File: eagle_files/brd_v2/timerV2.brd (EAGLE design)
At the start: 99.4 x 44.6 mm, 46 parts, among them IC1 7805T, IC6 DS1307, U1 ATMEGA328P

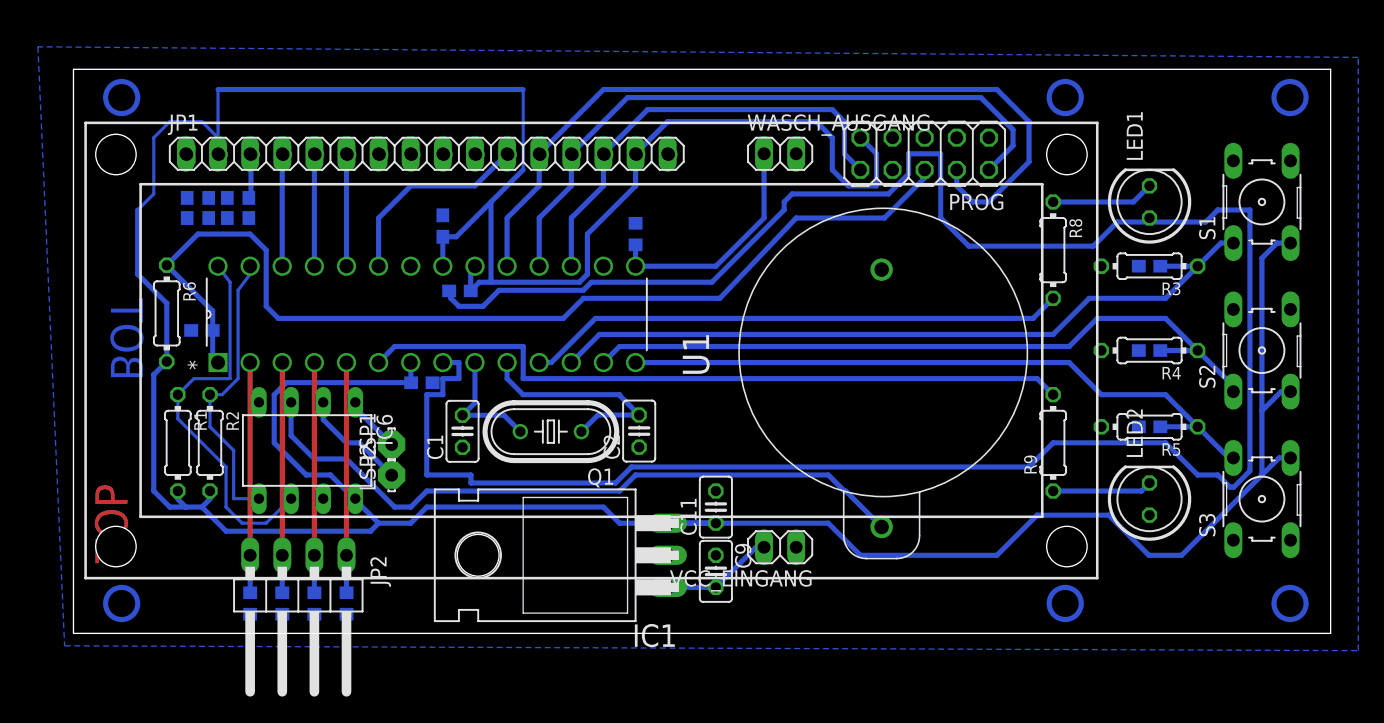
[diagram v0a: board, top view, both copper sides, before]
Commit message: added more input pins removed voltage regulator added pinheader
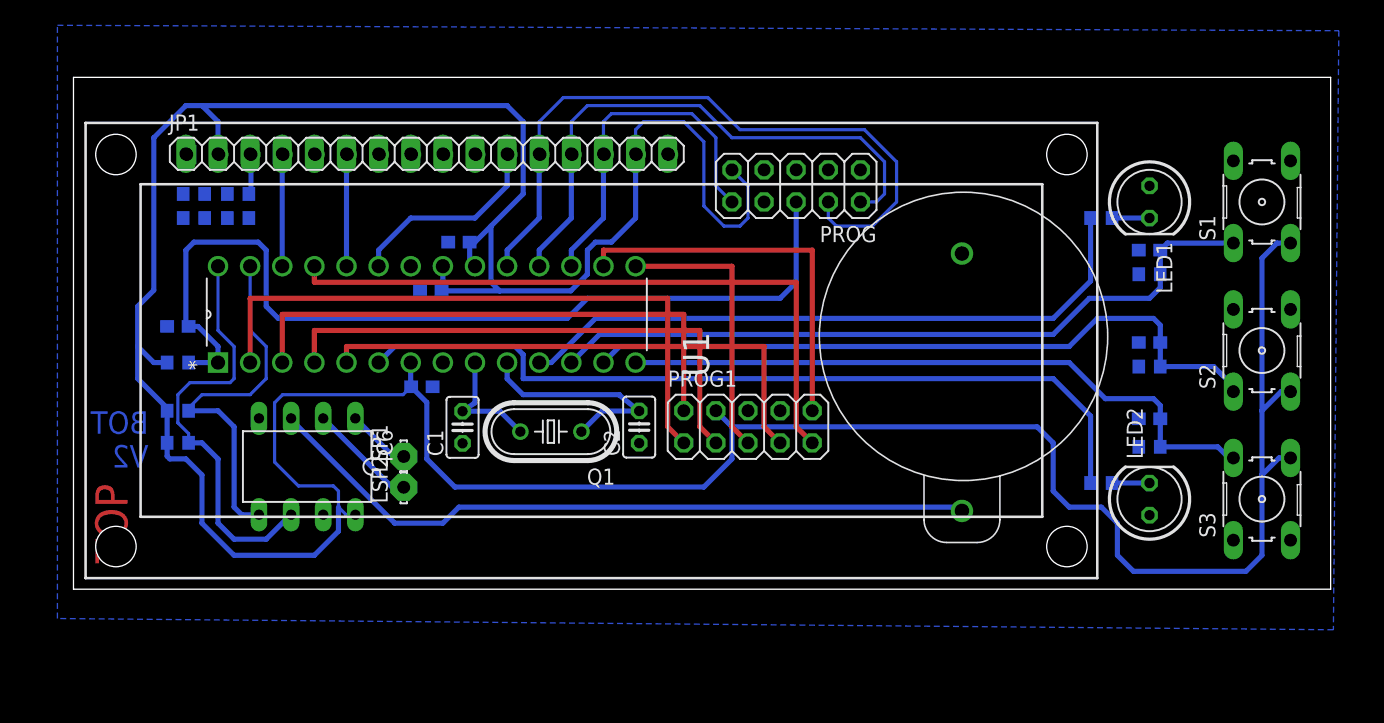
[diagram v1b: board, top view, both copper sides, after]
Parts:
- removed C11: 22 uF, resistor:C025-025X050
- removed C9: 22uF, resistor:C025-025X050
- removed IC1: 7805T, linear:TO220H
- removed JP2: (no value), pinhead:1X04/90
- removed R14, R15, R16, R17, R7: (no value), eagle-ltspice:R0603
- removed R9: 10k, resistor:0204/7
- removed VCC_EINGANG, WASCH_AUSGANG: (no value), pinhead:1X02
- added PROG1: (no value), pinhead:2X05
- added R20: (no value), eagle-ltspice:R0603
- R1, R2, R3, R4, R6: value 10k -> (none); device resistor:0204/7 -> eagle-ltspice:R0603
- R5, R8: value 10k -> 105; device resistor:0204/7 -> eagle-ltspice:R0603
- moved R6 77.8 mm to (86.4, 28.6), flipped to the bottom, turned to 0 degrees
- moved PROG 10.5 mm to (58.4, 35.6)
- moved R3 7.94 mm to (86.4, 21.3), flipped to the bottom, turned to 0 degrees
- moved R4 7.62 mm to (86.4, 14.9), flipped to the bottom, turned to 0 degrees
- moved U$1 6.48 mm to (71.5, 24.9)
- moved R1 6.35 mm to (9.53, 21.6), flipped to the bottom, turned to 180 degrees
- moved R5 5.85 mm to (82.5, 12.1), flipped to the bottom
- moved C10 5.17 mm to (29.5, 27.3), turned to 0 degrees
- moved R8 4.58 mm to (82.5, 33.0), flipped to the bottom, turned to 180 degrees
- moved C4 3.86 mm to (31.8, 31.1)
- moved R2 3.59 mm to (9.53, 17.8), flipped to the bottom, turned to 180 degrees
- moved C3 1.93 mm to (9.53, 24.4)
- moved LSP1 1.35 mm to (27.4, 14.2)
- moved LSP2 1.35 mm to (27.4, 11.7)
- moved C6 1.27 mm to (86.4, 30.5)
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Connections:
- removed net N$7: C9.2, IC1.1, VCC_EINGANG.2
- new net N$6: PROG1.10, U1.16
- net GND: now also JP1.5, PROG1.6, R6.2, U$2.5; no longer C11.2, C9.1, IC1.2, R14.1, R15.1, R16.1, R17.1, R5.2, R7.2, VCC_EINGANG.1, WASCH_AUSGANG.2
- net N$1: now also LED2.K, R5.2; no longer LED1.K, R8.1
- net N$11: now also R4.1; no longer R5.1
- net N$12: now also PROG1.7; no longer JP2.1, R17.2
- net N$13: now also R8.1; no longer R8.2
- net N$14: now also R5.1; no longer R9.2
- net N$15: now also PROG1.1; no longer JP2.4, R14.2
- net N$17: now also PROG1.3; no longer JP2.2, R16.2
- net N$20: now also R6.1; no longer R3.1
- net N$3: now also PROG1.5; no longer R7.1, WASCH_AUSGANG.1
- net N$39: now also R20.2; no longer R1.1
- net N$4: now also LED1.K, R8.2; no longer LED2.K, R9.1
- net N$40: now also R2.2; no longer R2.1
- net N$5: now also R1.2; no longer R6.1
- net N$8: now also R3.1; no longer R4.1
- net N$9: now also PROG1.2; no longer JP2.3, R15.2
- net RW: now also PROG1.9; no longer JP1.5, U$2.5
- net VCC: now also PROG1.4, R1.1, R2.1, R20.1; no longer C11.1, IC1.3, R1.2, R2.2, R6.2
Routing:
- net GND: track 179.9 -> 0.00 mm
- net RW: track 8.98 -> 52.6 mm
- net N$15: track 18.2 -> 50.1 mm
- net N$6: track 0.00 -> 30.5 mm
- net N$9: track 18.2 -> 43.2 mm
- net N$17: track 18.2 -> 42.4 mm
- net N$12: track 18.2 -> 42.4 mm
- net DB5: track 63.9 -> 54.6 mm
- net N$7: track 8.94 -> 0.00 mm
- net N$14: track 56.9 -> 65.5 mm
- net N$13: track 42.7 -> 51.3 mm
- net DB6: track 51.8 -> 44.4 mm
- net N$5: track 81.0 -> 73.9 mm
- net DB7: track 35.3 -> 28.1 mm
- net N$40: track 23.0 -> 29.4 mm
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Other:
- board size 99.4 x 44.6 mm -> 99.4 x 40.5 mm
- board text added: "BOT V2"
- board text removed: "BOT"

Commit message: Added Pulldown resistors for input pins
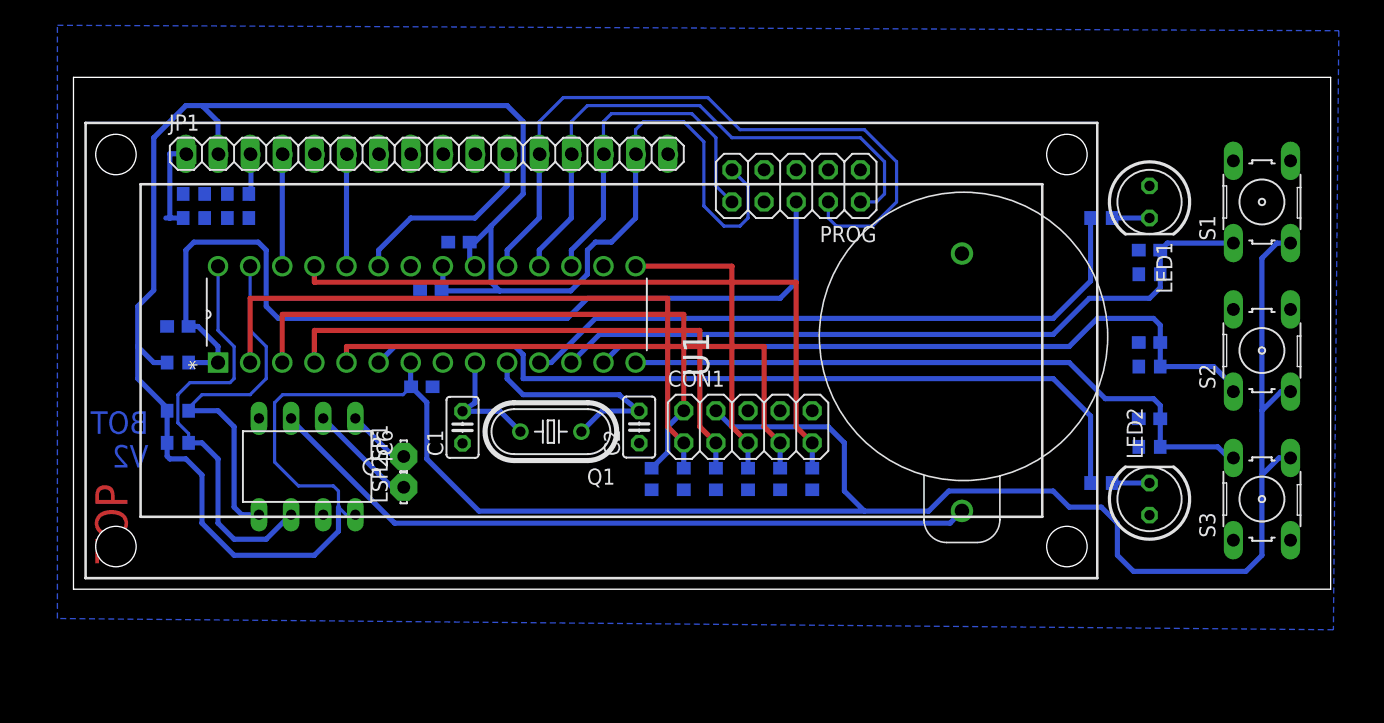
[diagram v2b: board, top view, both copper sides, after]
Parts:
- added R14, R15, R16, R17, R7, R9: 105, eagle-ltspice:R0603
- renumbered PROG1 to CON1
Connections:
- removed net N$6: CON1.10, U1.16
- net GND: now also R14.2, R15.2, R16.2, R17.2, R7.2, R9.2
- net N$12: now also R9.1
- net N$15: now also R16.1
- net N$17: now also R14.1
- net N$3: now also R17.1
- net N$9: now also R15.1
- net RW: now also R7.1
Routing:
- net N$6: track 30.5 -> 0.00 mm
- net VCC: track 300.2 -> 309.3 mm
- net GND: track 0.00 -> 7.72 mm
- net N$9: track 43.2 -> 48.8 mm
- net RW: track 52.6 -> 54.6 mm
- net N$3: track 22.1 -> 24.1 mm
- net N$17: track 42.4 -> 44.4 mm
- net N$15: track 50.1 -> 52.1 mm
- net N$12: track 42.4 -> 44.4 mm

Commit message: changed board layout
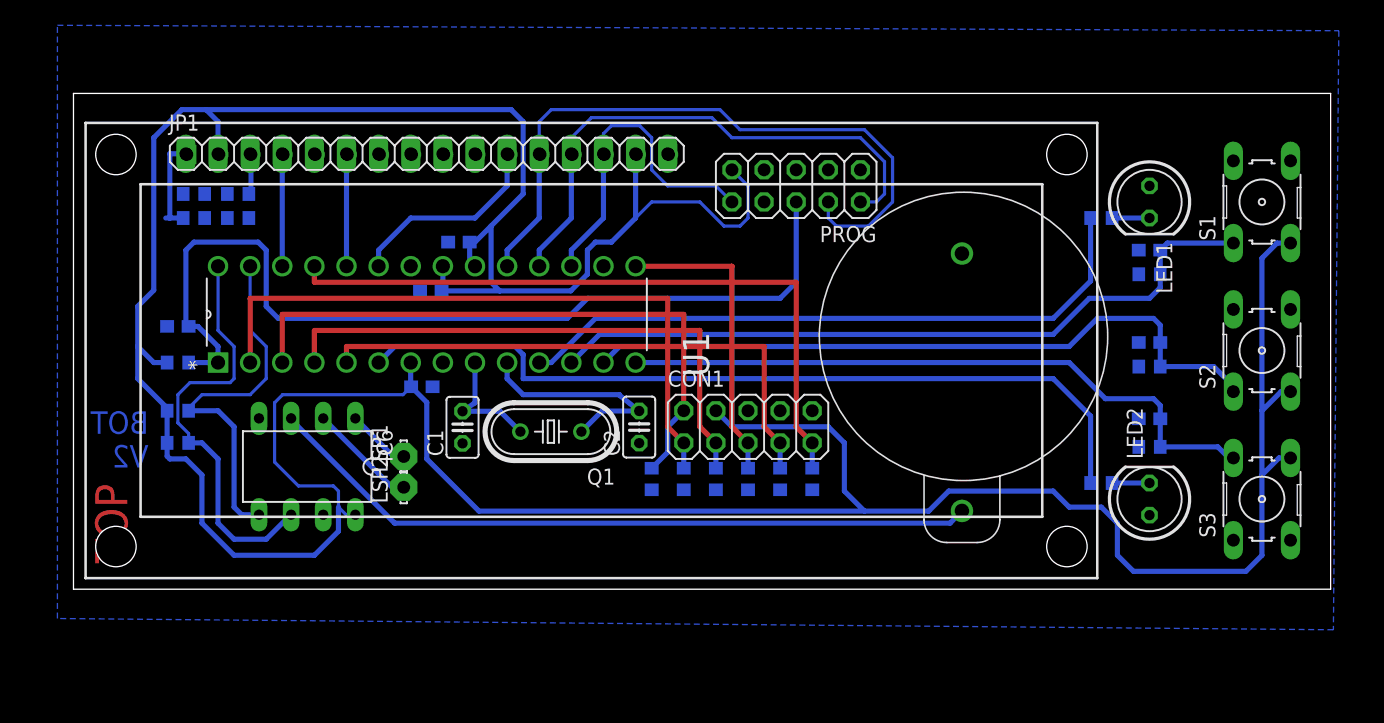
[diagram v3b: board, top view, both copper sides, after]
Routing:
- net VCC: track 309.3 -> 301.4 mm
- net DB7: track 28.1 -> 26.0 mm
- net DB6: track 44.4 -> 42.9 mm
- net DB5: track 54.6 -> 53.4 mm
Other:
- board size 99.4 x 40.5 mm -> 99.4 x 39.2 mm
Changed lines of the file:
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@@
 <layer number="19" name="Unrouted" color="6" fill="1" visible="yes" active="yes"/>
 <layer number="20" name="Dimension" color="15" fill="1" visible="yes" active="yes"/>
-<layer number="21" name="tPlace" color="7" fill="1" visible="yes" active="yes"/>
+<layer number="21" name="tPlace" color="7" fill="1" visible="no" active="yes"/>
 <layer number="22" name="bPlace" color="7" fill="1" visible="yes" active="yes"/>
 <layer number="23" name="tOrigins" color="15" fill="1" visible="yes" active="yes"/>
@@
 <board>
 <plain>
-<wire x1="100.6825" y1="3.6675" x2="100.6825" y2="44.1425" width="0" layer="20"/>
-<wire x1="100.6825" y1="44.1425" x2="1.27" y2="44.1425" width="0" layer="20"/>
-<wire x1="1.27" y1="44.1425" x2="1.27" y2="3.6675" width="0" layer="20"/>
+<wire x1="100.6825" y1="3.6675" x2="100.6825" y2="42.8725" width="0" layer="20"/>
+<wire x1="100.6825" y1="42.8725" x2="1.27" y2="42.8725" width="0" layer="20"/>
+<wire x1="1.27" y1="42.8725" x2="1.27" y2="3.6675" width="0" layer="20"/>
 <wire x1="1.27" y1="3.6675" x2="100.6825" y2="3.6675" width="0" layer="20"/>
 <text x="3" y="12" size="2.54" layer="1" font="vector" rot="R270">TOP</text>
@@
 <wire x1="41.91" y1="28.575" x2="41.91" y2="30.48" width="0.4064" layer="16"/>
 <wire x1="36.83" y1="34.925" x2="36.83" y2="40.64" width="0.4064" layer="16"/>
-<wire x1="36.83" y1="40.64" x2="35.56" y2="41.91" width="0.4064" layer="16"/>
-<wire x1="35.56" y1="41.91" x2="11.43" y2="41.91" width="0.4064" layer="16"/>
+<wire x1="36.83" y1="40.64" x2="35.8775" y2="41.5925" width="0.4064" layer="16"/>
+<wire x1="35.8775" y1="41.5925" x2="11.7475" y2="41.5925" width="0.4064" layer="16"/>
 <contactref element="R20" pad="1"/>
 <contactref element="R1" pad="1"/>
 <contactref element="R2" pad="1"/>
-<wire x1="11.43" y1="41.91" x2="10.16" y2="41.91" width="0.4064" layer="16"/>
+<wire x1="11.7475" y1="41.5925" x2="9.8425" y2="41.5925" width="0.4064" layer="16"/>
 <wire x1="6.35" y1="26.035" x2="6.35" y2="22.86" width="0.4064" layer="16"/>
 <wire x1="6.35" y1="22.86" x2="6.35" y2="20.32" width="0.4064" layer="16"/>
@@
 <wire x1="7.62" y1="39.37" x2="7.62" y2="27.305" width="0.4064" layer="16"/>
 <wire x1="7.62" y1="27.305" x2="6.35" y2="26.035" width="0.4064" layer="16"/>
-<wire x1="7.62" y1="39.37" x2="10.16" y2="41.91" width="0.4064" layer="16"/>
+<wire x1="7.62" y1="39.37" x2="9.8425" y2="41.5925" width="0.4064" layer="16"/>
 <wire x1="40.5925" y1="27.2575" x2="41.91" y2="28.575" width="0.4064" layer="16"/>
 <wire x1="40.5925" y1="27.2575" x2="34.9725" y2="27.2575" width="0.4064" layer="16"/>
@@
 <wire x1="17.17349375" y1="18.41553125" x2="17.17349375" y2="13.7212375" width="0.254" layer="16"/>
 <wire x1="17.17349375" y1="13.7212375" x2="19.061359375" y2="11.833371875" width="0.254" layer="16"/>
-<wire x1="45.7875" y1="38.0425" x2="45.7775" y2="38.0425" width="0.4064" layer="16"/>
 <wire x1="45.7775" y1="38.0425" x2="45.72" y2="38.1" width="0.4064" layer="16"/>
 <contactref element="CON1" pad="4"/>
@@
 <wire x1="8.675" y1="17.995" x2="6.35" y2="20.32" width="0.4064" layer="16"/>
 <wire x1="12.7" y1="38.1" x2="12.7" y2="40.64" width="0.4064" layer="16"/>
-<wire x1="12.7" y1="40.64" x2="11.43" y2="41.91" width="0.4064" layer="16"/>
+<wire x1="12.7" y1="40.64" x2="11.7475" y2="41.5925" width="0.4064" layer="16"/>
 <wire x1="12.7" y1="38.1" x2="12.71" y2="38.1" width="0.4064" layer="16"/>
 <wire x1="12.71" y1="38.1" x2="12.7675" y2="38.0425" width="0.4064" layer="16"/>
 <wire x1="8.675" y1="15.24" x2="8.675" y2="17.78" width="0.4064" layer="16"/>
-<wire x1="45.72" y1="38.1" x2="45.72" y2="40.005" width="0.254" layer="16"/>
-<wire x1="45.72" y1="40.005" x2="46.355" y2="40.64" width="0.254" layer="16"/>
-<wire x1="46.355" y1="40.64" x2="49.53" y2="40.64" width="0.254" layer="16"/>
-<wire x1="49.53" y1="40.64" x2="51.1175" y2="39.0525" width="0.254" layer="16"/>
-<wire x1="51.1175" y1="39.0525" x2="51.1175" y2="33.9725" width="0.254" layer="16"/>
-<wire x1="51.1175" y1="33.9725" x2="52.705" y2="32.385" width="0.254" layer="16"/>
+<wire x1="46.99" y1="34.29" x2="50.8" y2="34.29" width="0.254" layer="16"/>
+<wire x1="50.8" y1="34.29" x2="52.705" y2="32.385" width="0.254" layer="16"/>
 <wire x1="52.705" y1="32.385" x2="53.975" y2="32.385" width="0.254" layer="16"/>
 <wire x1="53.975" y1="32.385" x2="54.61" y2="33.02" width="0.254" layer="16"/>
@@
 <wire x1="8.89" y1="13.97" x2="10.16" y2="13.97" width="0.4064" layer="16"/>
 <wire x1="10.16" y1="13.97" x2="11.43" y2="12.7" width="0.4064" layer="16"/>
+<wire x1="46.99" y1="34.29" x2="45.72" y2="33.02" width="0.254" layer="16"/>
+<wire x1="45.7775" y1="38.0425" x2="45.7875" y2="38.0425" width="0" layer="19" extent="16-16"/>
 </signal>
 <signal name="GND">
@@
 <wire x1="38.1575" y1="38.0425" x2="38.1" y2="38.1" width="0.4064" layer="16"/>
 <wire x1="38.1" y1="38.1" x2="38.1" y2="40.64" width="0.254" layer="16"/>
-<wire x1="38.1" y1="40.64" x2="40.005" y2="42.545" width="0.254" layer="16"/>
-<wire x1="40.005" y1="42.545" x2="51.435" y2="42.545" width="0.254" layer="16"/>
-<wire x1="51.435" y1="42.545" x2="53.975" y2="40.005" width="0.254" layer="16"/>
-<wire x1="53.975" y1="40.005" x2="63.8175" y2="40.005" width="0.254" layer="16"/>
-<wire x1="63.8175" y1="40.005" x2="66.3575" y2="37.465" width="0.254" layer="16"/>
-<wire x1="66.3575" y1="37.465" x2="66.3575" y2="34.29" width="0.254" layer="16"/>
-<wire x1="66.3575" y1="34.29" x2="64.4525" y2="32.385" width="0.254" layer="16"/>
-<wire x1="64.4525" y1="32.385" x2="61.595" y2="32.385" width="0.254" layer="16"/>
+<wire x1="38.1" y1="40.64" x2="39.0525" y2="41.5925" width="0.254" layer="16"/>
+<wire x1="39.0525" y1="41.5925" x2="52.3875" y2="41.5925" width="0.254" layer="16"/>
+<wire x1="52.3875" y1="41.5925" x2="53.975" y2="40.005" width="0.254" layer="16"/>
+<wire x1="66.04" y1="34.29" x2="64.135" y2="32.385" width="0.254" layer="16"/>
+<wire x1="64.135" y1="32.385" x2="61.595" y2="32.385" width="0.254" layer="16"/>
 <wire x1="61.595" y1="32.385" x2="60.96" y2="33.02" width="0.254" layer="16"/>
 <wire x1="60.96" y1="33.02" x2="60.96" y2="34.29" width="0.254" layer="16"/>
+<wire x1="66.04" y1="34.29" x2="66.04" y2="37.7825" width="0.254" layer="16"/>
+<wire x1="66.04" y1="37.7825" x2="63.8175" y2="40.005" width="0.254" layer="16"/>
+<wire x1="63.8175" y1="40.005" x2="53.975" y2="40.005" width="0.254" layer="16"/>
 </signal>
 <signal name="DB6">
@@
 <wire x1="40.64" y1="38.1" x2="40.65" y2="38.1" width="0.4064" layer="16"/>
 <wire x1="40.65" y1="38.1" x2="40.7075" y2="38.0425" width="0.4064" layer="16"/>
-<wire x1="40.64" y1="40.64" x2="41.91" y2="41.91" width="0.254" layer="16"/>
-<wire x1="41.91" y1="41.91" x2="50.8" y2="41.91" width="0.254" layer="16"/>
-<wire x1="50.8" y1="41.91" x2="53.34" y2="39.37" width="0.254" layer="16"/>
+<wire x1="51.7525" y1="40.9575" x2="53.34" y2="39.37" width="0.254" layer="16"/>
 <wire x1="53.34" y1="39.37" x2="63.5" y2="39.37" width="0.254" layer="16"/>
 <wire x1="63.5" y1="39.37" x2="65.405" y2="37.465" width="0.254" layer="16"/>
@@
 <wire x1="65.405" y1="34.925" x2="64.77" y2="34.29" width="0.254" layer="16"/>
 <wire x1="64.77" y1="34.29" x2="63.5" y2="34.29" width="0.254" layer="16"/>
-<wire x1="40.64" y1="40.64" x2="40.64" y2="38.1" width="0.254" layer="16"/>
+<wire x1="40.64" y1="38.1" x2="40.64" y2="39.37" width="0.254" layer="16"/>
+<wire x1="40.64" y1="39.37" x2="42.2275" y2="40.9575" width="0.254" layer="16"/>
+<wire x1="42.2275" y1="40.9575" x2="51.7525" y2="40.9575" width="0.254" layer="16"/>
 </signal>
 <signal name="DB7">
@@
 <wire x1="40.64" y1="30.48" x2="43.18" y2="33.02" width="0.4064" layer="16"/>
 <wire x1="43.18" y1="33.02" x2="43.18" y2="38.1" width="0.4064" layer="16"/>
-<wire x1="43.18" y1="38.1" x2="43.18" y2="40.64" width="0.254" layer="16"/>
-<wire x1="43.18" y1="40.64" x2="43.815" y2="41.275" width="0.254" layer="16"/>
-<wire x1="43.815" y1="41.275" x2="50.165" y2="41.275" width="0.254" layer="16"/>
-<wire x1="50.165" y1="41.275" x2="52.07" y2="39.37" width="0.254" layer="16"/>
-<wire x1="52.07" y1="39.37" x2="52.07" y2="35.56" width="0.254" layer="16"/>
+<wire x1="43.18" y1="38.1" x2="43.18" y2="39.6875" width="0.254" layer="16"/>
+<wire x1="43.18" y1="39.6875" x2="43.815" y2="40.3225" width="0.254" layer="16"/>
 <wire x1="52.07" y1="35.56" x2="53.34" y2="34.29" width="0.254" layer="16"/>
+<wire x1="43.815" y1="40.3225" x2="46.0375" y2="40.3225" width="0.254" layer="16"/>
+<wire x1="46.0375" y1="40.3225" x2="46.99" y2="39.37" width="0.254" layer="16"/>
+<wire x1="46.99" y1="39.37" x2="46.99" y2="36.83" width="0.254" layer="16"/>
+<wire x1="46.99" y1="36.83" x2="48.26" y2="35.56" width="0.254" layer="16"/>
+<wire x1="48.26" y1="35.56" x2="52.07" y2="35.56" width="0.254" layer="16"/>
 </signal>
 <signal name="N$20">
